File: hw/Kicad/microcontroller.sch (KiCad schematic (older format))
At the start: 44 parts, among them J301 Conn_display, J302 Conn_expansion, J303 Conn_E3Z-D62, Q301 TSM2312CX, SW301 SW_Push, SW302 SW_Push, SW303 SW_Push, SW304 SW_Push, U301 CP2102N-A01-GQFN28, U302 ESP32-WROOM-32

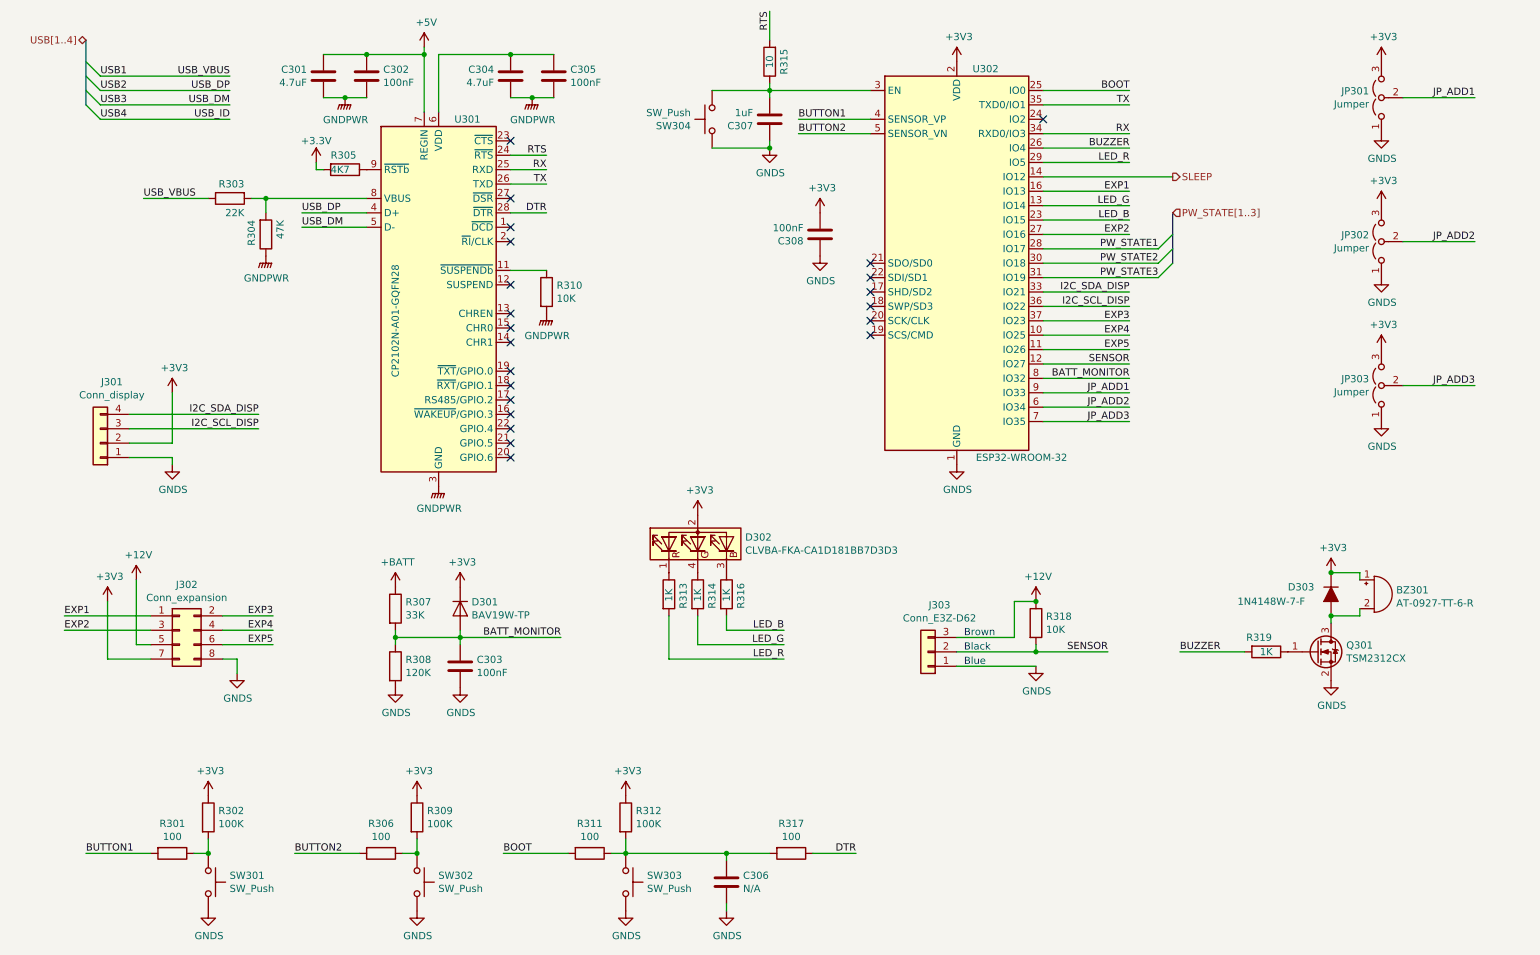
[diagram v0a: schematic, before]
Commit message: V1.1 version. UART fixed and some signals renamed
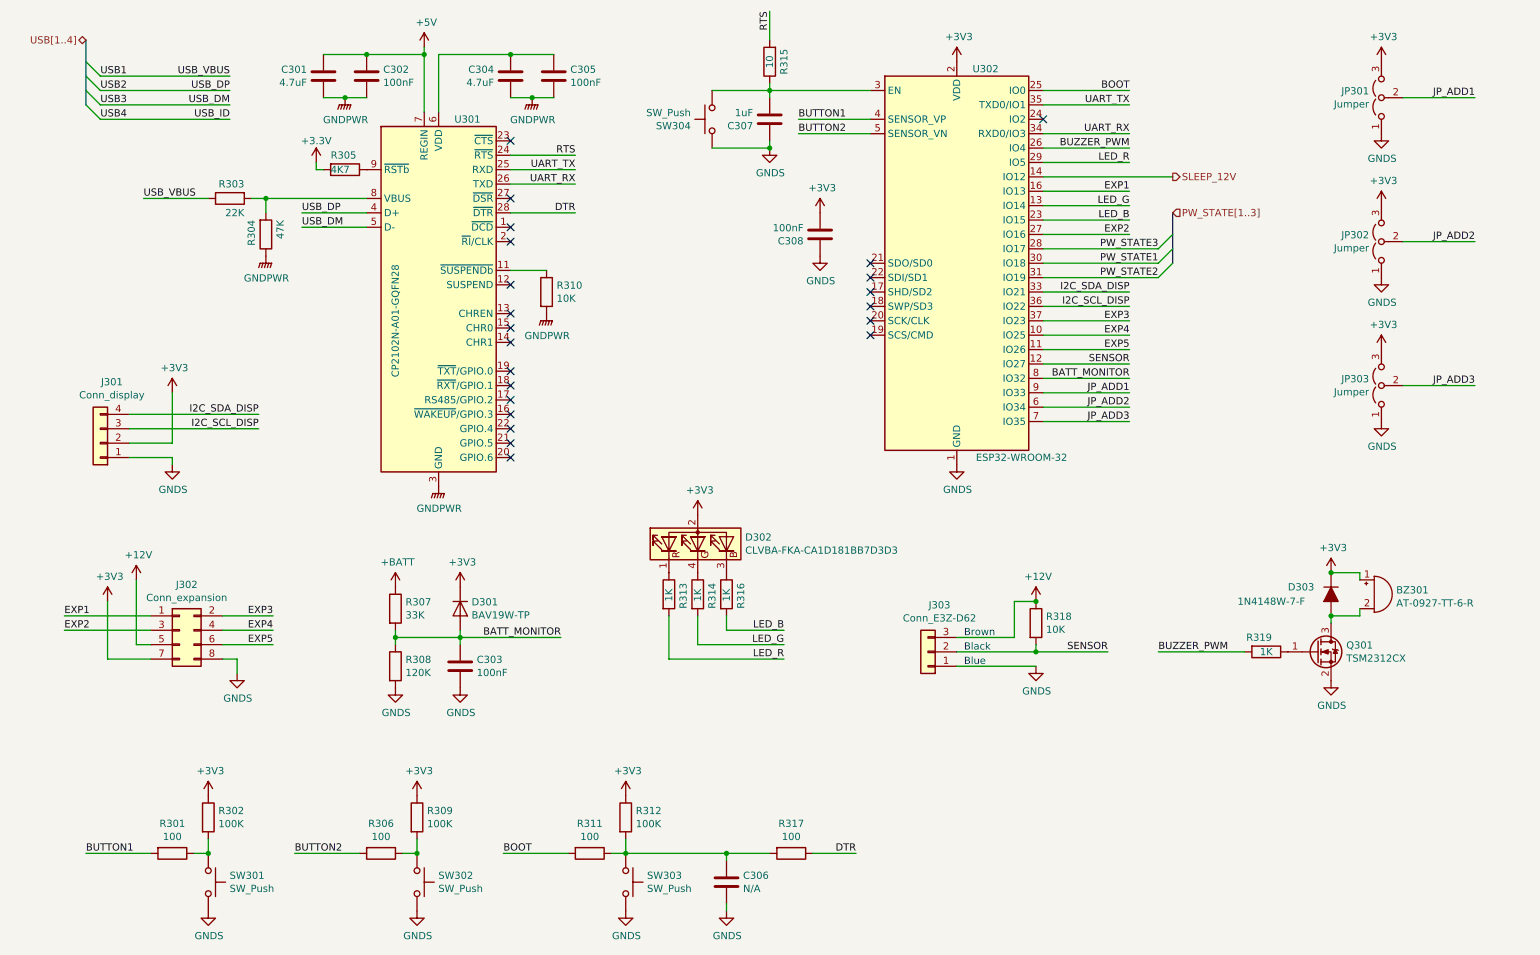
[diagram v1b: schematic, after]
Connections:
- net PW_STATE1: now also U302.30 (IO18); no longer U302.28 (IO17)
- net PW_STATE2: now also U302.31 (IO19); no longer U302.30 (IO18)
- net PW_STATE3: now also U302.28 (IO17); no longer U302.31 (IO19)
- net BUZZER renamed BUZZER_PWM
- net RX renamed UART_RX
- net UART_RX: now also U301.26 (TXD); no longer U301.25 (RXD)
- net SLEEP renamed SLEEP_12V
- net TX renamed UART_TX
- net UART_TX: now also U301.25 (RXD); no longer U301.26 (TXD)
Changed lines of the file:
@@
 Sheet 3 3
 Title "time2time project"
-Date "2019-09-09"
-Rev "V1.0"
+Date "2019-10-29"
+Rev "V1.1"
 Comp "Puma Pride Robotics Team"
 Comment1 "Designed by Rubén Espino San José"
@@
 JP_ADD3
 Wire Wire Line
-	9150 5400 8700 5400
-Text Label 8700 5400 0    50   ~ 0
-BUZZER
+	9150 5400 8550 5400
+Text Label 8550 5400 0    50   ~ 0
+BUZZER_PWM
 $Comp
 L Connector_Generic:Conn_01x03 J303
@@
 	6050 1800 6550 1800
 Text Label 8350 1600 2    50   ~ 0
-TX
+UART_TX
 Text Label 8350 1800 2    50   ~ 0
-RX
+UART_RX
 $Comp
 L Interface_USB:CP2102N-A01-GQFN28 U?
@@
 	3450 1650 3450 1250
 Wire Wire Line
-	4300 2050 4050 2050
-Wire Wire Line
-	4300 2150 4050 2150
+	4500 2050 4050 2050
+Wire Wire Line
+	4500 2150 4050 2150
 $Comp
 L Device:C C?
@@
 NoConn ~ 4050 3050
 NoConn ~ 4050 3150
-Text Label 4300 2050 2    50   ~ 0
-RX
-Text Label 4300 2150 2    50   ~ 0
-TX
+Text Label 4500 2150 2    50   ~ 0
+UART_RX
+Text Label 4500 2050 2    50   ~ 0
+UART_TX
 Text HLabel 1100 1150 0    50   BiDi ~ 0
 USB[1..4]
@@
 LED_B
 Text Label 8350 1900 2    50   ~ 0
-BUZZER
+BUZZER_PWM
 Text Label 8350 3600 2    50   ~ 0
 JP_ADD1
@@
 Text HLabel 8650 2350 2    50   Input ~ 0
 PW_STATE[1..3]
+Text Label 8550 2700 2    50   ~ 0
+PW_STATE1
+Text Label 8550 2800 2    50   ~ 0
+PW_STATE2
 Text Label 8550 2600 2    50   ~ 0
-PW_STATE1
-Text Label 8550 2700 2    50   ~ 0
-PW_STATE2
-Text Label 8550 2800 2    50   ~ 0
 PW_STATE3
 Text Label 1200 1400 0    50   ~ 0
@@
 	7750 2100 8650 2100
 Text HLabel 8650 2100 2    50   Output ~ 0
-SLEEP
+SLEEP_12V
 $Comp
 L Switch:SW_Push SW302
@@
 $EndComp
 Wire Wire Line
-	4050 1950 4300 1950
-Wire Wire Line
-	4050 2350 4300 2350
-Text Label 4300 1950 2    50   ~ 0
+	4050 1950 4500 1950
+Wire Wire Line
+	4050 2350 4500 2350
+Text Label 4500 1950 2    50   ~ 0
 RTS
-Text Label 4300 2350 2    50   ~ 0
+Text Label 4500 2350 2    50   ~ 0
 DTR
 $Comp
@@
 	0    -1   1    0
 $EndComp
+Connection ~ 9750 4850
+Connection ~ 9750 5150
 Wire Bus Line
 	8650 2350 8650 2700
 Wire Bus Line
 	1100 1150 1100 1600
-Connection ~ 9750 4850
-Connection ~ 9750 5150
 $EndSCHEMATC

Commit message: Resistor value changed for ADC battery monitor
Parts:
- R307: value 33K -> 47K
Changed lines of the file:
@@
 Sheet 3 3
 Title "time2time project"
-Date "2019-10-29"
+Date "2019-10-30"
 Rev "V1.1"
 Comp "Puma Pride Robotics Team"
@@
 P 3250 5100
 F 0 "R307" H 3320 5146 50  0000 L CNN
-F 1 "33K" H 3320 5055 50  0000 L CNN
+F 1 "47K" H 3320 5055 50  0000 L CNN
 F 2 "Resistor_SMD:R_0603_1608Metric" V 3180 5100 50  0001 C CNN
 F 3 "~" H 3250 5100 50  0001 C CNN

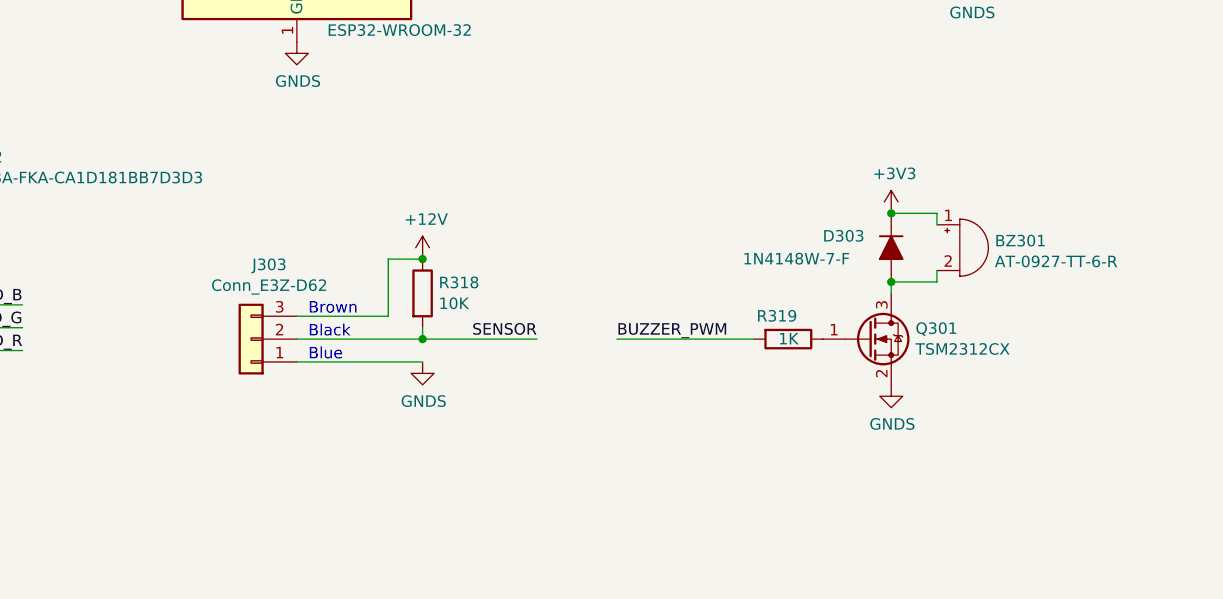
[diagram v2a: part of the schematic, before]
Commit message: t2t_fw. Add schottky diode to prevent the ESP32 sensor pin from exced 3V3
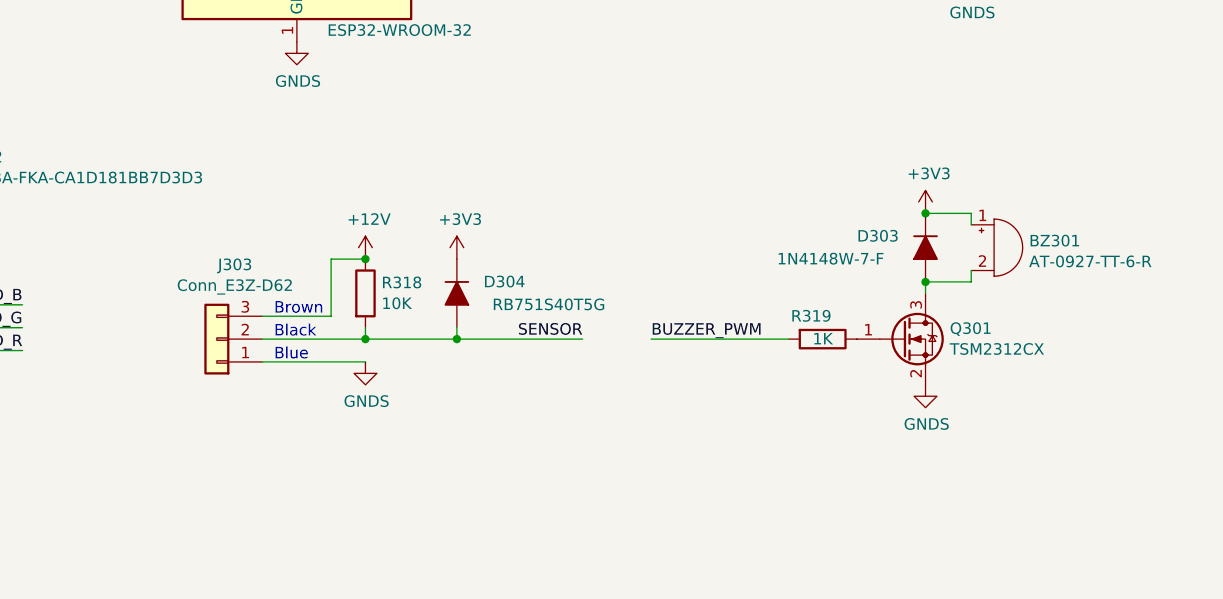
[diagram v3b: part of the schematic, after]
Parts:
- added D304: RB751S40T5G, Diode_SMD:D_SOD-523, symbol Device:D_ALT
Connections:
- net +3V3: now also D304.1 (K)
- net SENSOR: now also D304.2 (A)
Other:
- moved on the sheet: BZ301, D303, J303, Q301, R318, R319
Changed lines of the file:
@@
 EESchema Schematic File Version 4
-LIBS:time2time-cache
-EELAYER 26 0
+EELAYER 30 0
 EELAYER END
 $Descr A4 11693 8268
@@
 Sheet 3 3
 Title "time2time project"
-Date "2019-10-30"
+Date "2021-02-28"
 Rev "V1.1"
 Comp "Puma Pride Robotics Team"
@@
 L Device:Q_NMOS_GSD Q301
 U 1 1 5CD47D16
-P 9650 5400
-F 0 "Q301" H 9856 5446 50  0000 L CNN
-F 1 "TSM2312CX" H 9856 5355 50  0000 L CNN
-F 2 "Package_TO_SOT_SMD:SOT-23" H 9850 5500 50  0001 C CNN
-F 3 "~" H 9650 5400 50  0001 C CNN
-	1    9650 5400
+P 9800 5400
+F 0 "Q301" H 10006 5446 50  0000 L CNN
+F 1 "TSM2312CX" H 10006 5355 50  0000 L CNN
+F 2 "Package_TO_SOT_SMD:SOT-23" H 10000 5500 50  0001 C CNN
+F 3 "~" H 9800 5400 50  0001 C CNN
+	1    9800 5400
 	1    0    0    -1
 $EndComp
@@
 L Device:R R319
 U 1 1 5CD47EFD
-P 9300 5400
-F 0 "R319" V 9200 5350 50  0000 C CNN
-F 1 "1K" V 9300 5400 50  0000 C CNN
-F 2 "Resistor_SMD:R_0603_1608Metric" V 9230 5400 50  0001 C CNN
-F 3 "~" H 9300 5400 50  0001 C CNN
-	1    9300 5400
+P 9450 5400
+F 0 "R319" V 9350 5350 50  0000 C CNN
+F 1 "1K" V 9450 5400 50  0000 C CNN
+F 2 "Resistor_SMD:R_0603_1608Metric" V 9380 5400 50  0001 C CNN
+F 3 "~" H 9450 5400 50  0001 C CNN
+	1    9450 5400
 	0    1    1    0
 $EndComp
@@
 L Device:Buzzer BZ301
 U 1 1 5CD483B2
-P 10050 5000
-F 0 "BZ301" H 10203 5029 50  0000 L CNN
-F 1 "AT-0927-TT-6-R" H 10203 4938 50  0000 L CNN
-F 2 "Buzzer_Beeper:MagneticBuzzer_PUI_AT-0927-TT-6-R" V 10025 5100 50  0001 C CNN
-F 3 "~" V 10025 5100 50  0001 C CNN
-	1    10050 5000
+P 10200 5000
+F 0 "BZ301" H 10353 5029 50  0000 L CNN
+F 1 "AT-0927-TT-6-R" H 10353 4938 50  0000 L CNN
+F 2 "Buzzer_Beeper:MagneticBuzzer_PUI_AT-0927-TT-6-R" V 10175 5100 50  0001 C CNN
+F 3 "~" V 10175 5100 50  0001 C CNN
+	1    10200 5000
 	1    0    0    -1
 $EndComp
@@
 	5150 5450 5950 5450
 Wire Wire Line
-	9950 5100 9950 5150
-Wire Wire Line
-	9950 5150 9750 5150
-Wire Wire Line
-	9750 5200 9750 5150
-Wire Wire Line
-	9950 4900 9950 4850
-Wire Wire Line
-	9950 4850 9750 4850
+	10100 5100 10100 5150
+Wire Wire Line
+	10100 5150 9900 5150
+Wire Wire Line
+	9900 5200 9900 5150
+Wire Wire Line
+	10100 4900 10100 4850
+Wire Wire Line
+	10100 4850 9900 4850
 $Comp
 L power:+3V3 #PWR0332
 U 1 1 5CD4ADF3
-P 9750 4850
-F 0 "#PWR0332" H 9750 4700 50  0001 C CNN
-F 1 "+3V3" H 9765 5023 50  0000 C CNN
-F 2 "" H 9750 4850 50  0001 C CNN
-F 3 "" H 9750 4850 50  0001 C CNN
-	1    9750 4850
+P 9900 4850
+F 0 "#PWR0332" H 9900 4700 50  0001 C CNN
+F 1 "+3V3" H 9915 5023 50  0000 C CNN
+F 2 "" H 9900 4850 50  0001 C CNN
+F 3 "" H 9900 4850 50  0001 C CNN
+	1    9900 4850
 	1    0    0    -1
 $EndComp
@@
 JP_ADD3
 Wire Wire Line
-	9150 5400 8550 5400
-Text Label 8550 5400 0    50   ~ 0
+	9300 5400 8700 5400
+Text Label 8700 5400 0    50   ~ 0
 BUZZER_PWM
 $Comp
 L Connector_Generic:Conn_01x03 J303
 U 1 1 5D01B53A
-P 6950 5400
-F 0 "J303" H 6870 5075 50  0000 C CNN
-F 1 "Conn_E3Z-D62" H 6870 5166 50  0000 C CNN
-F 2 "Connector_PinSocket_2.54mm:PinSocket_1x03_P2.54mm_Vertical" H 6950 5400 50  0001 C CNN
-F 3 "~" H 6950 5400 50  0001 C CNN
-	1    6950 5400
+P 6800 5400
+F 0 "J303" H 6720 5075 50  0000 C CNN
+F 1 "Conn_E3Z-D62" H 6720 5166 50  0000 C CNN
+F 2 "Connector_PinSocket_2.54mm:PinSocket_1x03_P2.54mm_Vertical" H 6800 5400 50  0001 C CNN
+F 3 "~" H 6800 5400 50  0001 C CNN
+	1    6800 5400
 	-1   0    0    1
 $EndComp
@@
 L Device:R R318
 U 1 1 5D01BFFA
-P 7700 5200
-F 0 "R318" H 7770 5246 50  0000 L CNN
-F 1 "10K" H 7770 5155 50  0000 L CNN
-F 2 "Resistor_SMD:R_0603_1608Metric" V 7630 5200 50  0001 C CNN
-F 3 "~" H 7700 5200 50  0001 C CNN
-	1    7700 5200
+P 7450 5200
+F 0 "R318" H 7520 5246 50  0000 L CNN
+F 1 "10K" H 7520 5155 50  0000 L CNN
+F 2 "Resistor_SMD:R_0603_1608Metric" V 7380 5200 50  0001 C CNN
+F 3 "~" H 7450 5200 50  0001 C CNN
+	1    7450 5200
 	1    0    0    -1
 $EndComp
@@
 L power:+12V #PWR0330
 U 1 1 5D01C172
-P 7700 5050
-F 0 "#PWR0330" H 7700 4900 50  0001 C CNN
-F 1 "+12V" H 7715 5223 50  0000 C CNN
-F 2 "" H 7700 5050 50  0001 C CNN
-F 3 "" H 7700 5050 50  0001 C CNN
-	1    7700 5050
-	1    0    0    -1
-$EndComp
-Text Notes 7200 5300 0    50   ~ 0
+P 7450 5050
+F 0 "#PWR0330" H 7450 4900 50  0001 C CNN
+F 1 "+12V" H 7465 5223 50  0000 C CNN
+F 2 "" H 7450 5050 50  0001 C CNN
+F 3 "" H 7450 5050 50  0001 C CNN
+	1    7450 5050
+	1    0    0    -1
+$EndComp
+Text Notes 7050 5300 0    50   ~ 0
 Brown
-Text Notes 7200 5400 0    50   ~ 0
+Text Notes 7050 5400 0    50   ~ 0
 Black
-Text Notes 7200 5500 0    50   ~ 0
+Text Notes 7050 5500 0    50   ~ 0
 Blue
 Wire Wire Line
-	7700 5050 7550 5050
-Wire Wire Line
-	7550 5050 7550 5300
-Wire Wire Line
-	7550 5300 7150 5300
-Wire Wire Line
-	7150 5400 7700 5400
-Connection ~ 7700 5050
-Wire Wire Line
-	7700 5400 7700 5350
-Wire Wire Line
-	7700 5400 8200 5400
-Connection ~ 7700 5400
-Wire Wire Line
-	7150 5500 7700 5500
-Text Label 8200 5400 2    50   ~ 0
+	7450 5050 7300 5050
+Wire Wire Line
+	7300 5050 7300 5300
+Wire Wire Line
+	7300 5300 7000 5300
+Wire Wire Line
+	7000 5400 7450 5400
+Connection ~ 7450 5050
+Wire Wire Line
+	7450 5400 7450 5350
+Wire Wire Line
+	7450 5400 7850 5400
+Wire Wire Line
+	7000 5500 7450 5500
+Text Label 8400 5400 2    50   ~ 0
 SENSOR
 Wire Wire Line
@@
 L power:GNDS #PWR0111
 U 1 1 5D79C80F
-P 9750 5600
-F 0 "#PWR0111" H 9750 5350 50  0001 C CNN
-F 1 "GNDS" H 9755 5427 50  0000 C CNN
-F 2 "" H 9750 5600 50  0001 C CNN
-F 3 "" H 9750 5600 50  0001 C CNN
-	1    9750 5600
+P 9900 5600
+F 0 "#PWR0111" H 9900 5350 50  0001 C CNN
+F 1 "GNDS" H 9905 5427 50  0000 C CNN
+F 2 "" H 9900 5600 50  0001 C CNN
+F 3 "" H 9900 5600 50  0001 C CNN
+	1    9900 5600
 	1    0    0    -1
 $EndComp
@@
 L power:GNDS #PWR0112
 U 1 1 5D79C872
-P 7700 5500
-F 0 "#PWR0112" H 7700 5250 50  0001 C CNN
-F 1 "GNDS" H 7705 5327 50  0000 C CNN
-F 2 "" H 7700 5500 50  0001 C CNN
-F 3 "" H 7700 5500 50  0001 C CNN
-	1    7700 5500
+P 7450 5500
+F 0 "#PWR0112" H 7450 5250 50  0001 C CNN
+F 1 "GNDS" H 7455 5327 50  0000 C CNN
+F 2 "" H 7450 5500 50  0001 C CNN
+F 3 "" H 7450 5500 50  0001 C CNN
+	1    7450 5500
 	1    0    0    -1
 $EndComp
@@
 	1    0    0    -1
 $EndComp
-$Comp
-L Device:D_ALT D303
-U 1 1 5D76A848
-P 9750 5000
-F 0 "D303" V 9700 5300 50  0000 R CNN
-F 1 "1N4148W-7-F" V 9800 5650 50  0000 R CNN
-F 2 "Diode_SMD:D_SOD-123" H 9750 5000 50  0001 C CNN
-F 3 "~" H 9750 5000 50  0001 C CNN
-	1    9750 5000
-	0    -1   1    0
-$EndComp
-Connection ~ 9750 4850
-Connection ~ 9750 5150
+Connection ~ 7450 5400
+Wire Wire Line
+	7850 5350 7850 5400
+Connection ~ 7850 5400
+Wire Wire Line
+	7850 5400 8400 5400
+Connection ~ 9900 5150
+Connection ~ 9900 4850
 Wire Bus Line
 	8650 2350 8650 2700
 Wire Bus Line
 	1100 1150 1100 1600
+$Comp
+L Device:D_ALT D303
+U 1 1 5D76A848
+P 9900 5000
+F 0 "D303" V 9850 5300 50  0000 R CNN
+F 1 "1N4148W-7-F" V 9950 5650 50  0000 R CNN
+F 2 "Diode_SMD:D_SOD-123" H 9900 5000 50  0001 C CNN
+F 3 "~" H 9900 5000 50  0001 C CNN
+	1    9900 5000
+	0    -1   1    0
+$EndComp
+$Comp
+L Device:D_ALT D304
+U 1 1 604930E5
+P 7850 5200
+F 0 "D304" V 7800 5500 50  0000 R CNN
+F 1 "RB751S40T5G" V 7900 5850 50  0000 R CNN
+F 2 "Diode_SMD:D_SOD-523" H 7850 5200 50  0001 C CNN
+F 3 "~" H 7850 5200 50  0001 C CNN
+	1    7850 5200
+	0    1    1    0
+$EndComp
+$Comp
+L power:+3V3 #PWR0120
+U 1 1 605749FF
+P 7850 5050
+F 0 "#PWR0120" H 7850 4900 50  0001 C CNN
+F 1 "+3V3" H 7865 5223 50  0000 C CNN
+F 2 "" H 7850 5050 50  0001 C CNN
+F 3 "" H 7850 5050 50  0001 C CNN
+	1    7850 5050
+	1    0    0    -1
+$EndComp
 $EndSCHEMATC
